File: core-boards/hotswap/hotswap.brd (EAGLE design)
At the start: 59.7 x 56.8 mm, 16 parts, among them J1 WALL, J2 BATTERY, J3 COMPUTER, Q1 SUP75P03_07, Q2 SUP75P03_07, Q3 SUP75P03_07, U1 LTC4416EMS#PBF

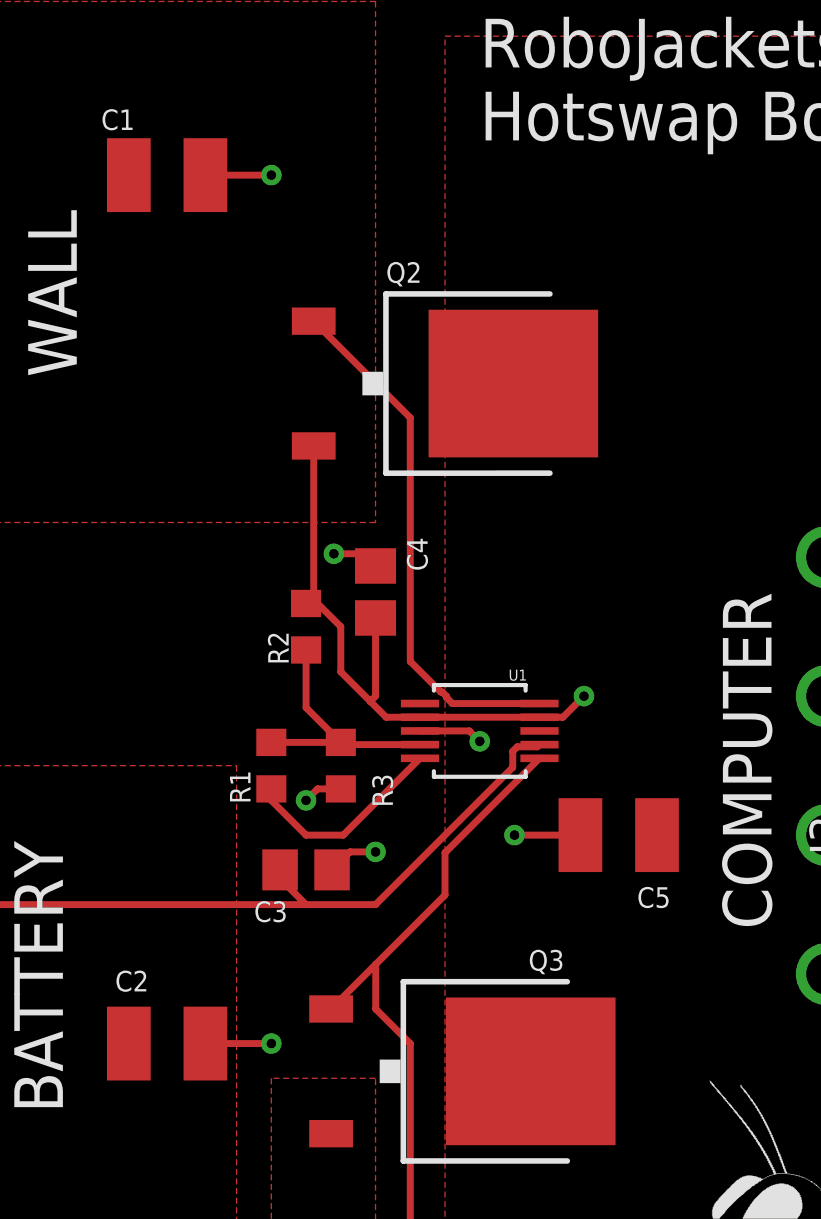
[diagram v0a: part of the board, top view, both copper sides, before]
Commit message: Flip transistor sides so voltage does not reverse flow from V2 to V1 when V2 is higher
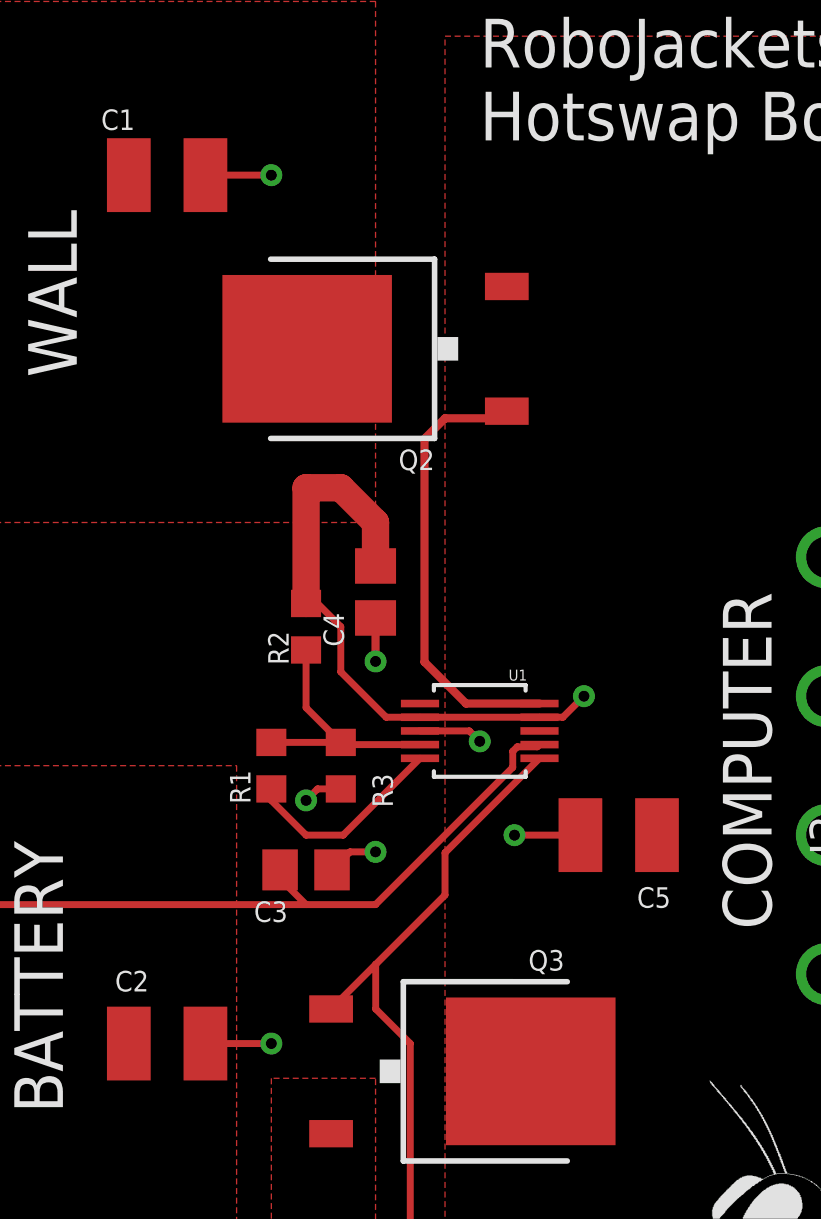
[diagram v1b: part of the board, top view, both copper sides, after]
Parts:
- moved Q2 2.84 mm to (29.2, 44.5), turned to 90 degrees
- turned C4 to 270 degrees
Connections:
- net VCC_COMP: now also Q2.S; no longer Q2.D
- net VCC_WALL: now also Q2.D; no longer Q2.S
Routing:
- net N$4: track 19.3 -> 16.4 mm
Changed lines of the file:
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@@
 <?xml version="1.0" encoding="utf-8"?>
 <!DOCTYPE eagle SYSTEM "eagle.dtd">
-<eagle version="9.3.0">
+<eagle version="9.4.2">
 <drawing>
 <settings>
@@
 <setting verticaltext="up"/>
 </settings>
-<grid distance="50" unitdist="mil" unit="mm" style="lines" multiple="1" display="no" altdistance="5" altunitdist="mil" altunit="mm"/>
+<grid distance="1" unitdist="mm" unit="mm" style="lines" multiple="1" display="no" altdistance="1" altunitdist="mm" altunit="mm"/>
 <layers>
 <layer number="1" name="Top" color="4" fill="1" visible="yes" active="yes"/>
@@
 <attribute name="SPICEPREFIX" value="R" x="154.94" y="71.12" size="1.778" layer="27" rot="R90" display="off"/>
 </element>
-<element name="Q2" library="IGVC-Discrete" package="DPACK_2" value="SUP75P03_07" x="31.75" y="43.18" smashed="yes" rot="R270">
-<attribute name="NAME" x="29.591" y="46.863" size="0.75" layer="25"/>
+<element name="Q2" library="IGVC-Discrete" package="DPACK_2" value="SUP75P03_07" x="29.21" y="44.45" smashed="yes" rot="R90">
+<attribute name="NAME" x="31.369" y="40.767" size="0.75" layer="25" rot="R180"/>
 </element>
 <element name="Q3" library="IGVC-Discrete" package="DPACK_2" value="SUP75P03_07" x="32.385" y="18.034" smashed="yes" rot="R270">
@@
 <attribute name="SPICEPREFIX" value="C" x="38.1" y="26.67" size="1.778" layer="27" rot="R180" display="off"/>
 </element>
-<element name="C4" library="rcl" library_urn="urn:adsk.eagle:library:334" package="C0805" package3d_urn="urn:adsk.eagle:package:23617/2" value=".1uF" x="29.21" y="35.56" smashed="yes" rot="R90">
-<attribute name="NAME" x="31.115" y="36.322" size="0.75" layer="25" rot="R90"/>
-<attribute name="SPICEPREFIX" value="C" x="29.21" y="35.56" size="1.778" layer="27" rot="R90" display="off"/>
+<element name="C4" library="rcl" library_urn="urn:adsk.eagle:library:334" package="C0805" package3d_urn="urn:adsk.eagle:package:23617/2" value=".1uF" x="29.21" y="35.56" smashed="yes" rot="R270">
+<attribute name="NAME" x="27.305" y="34.798" size="0.75" layer="25" rot="R270"/>
+<attribute name="SPICEPREFIX" value="C" x="29.21" y="35.56" size="1.778" layer="27" rot="R270" display="off"/>
 </element>
 <element name="E$1" library="RoboJackets-Aesthetics" package="ROBOBUZZ_0.8X" value="" x="44.45" y="2.54" smashed="yes"/>
@@
 <wire x1="27.94" y1="28.36" x2="27.09" y2="28.36" width="0.254" layer="1"/>
 <wire x1="27.09" y1="28.36" x2="26.67" y2="27.94" width="0.254" layer="1"/>
-<via x="26.67" y="27.94" extent="1-16" drill="0.35"/>
+<via x="26.67" y="27.94" extent="1-16" drill="0.4"/>
 <wire x1="33.02" y1="30.099" x2="32.639" y2="30.48" width="0.254" layer="1"/>
 <wire x1="32.639" y1="30.48" x2="30.8356" y2="30.48" width="0.254" layer="1"/>
-<via x="33.02" y="30.099" extent="1-16" drill="0.35"/>
+<via x="33.02" y="30.099" extent="1-16" drill="0.4"/>
 <contactref element="C4" pad="2"/>
 <contactref element="J2" pad="4"/>
 <contactref element="J1" pad="4"/>
 <wire x1="36.7" y1="26.67" x2="34.29" y2="26.67" width="0.254" layer="1"/>
-<via x="34.29" y="26.67" extent="1-16" drill="0.35"/>
+<via x="34.29" y="26.67" extent="1-16" drill="0.4"/>
 <wire x1="29.21" y1="26.0576" x2="28.2776" y2="26.0576" width="0.254" layer="1"/>
 <wire x1="27.62" y1="25.4" x2="28.2776" y2="26.0576" width="0.254" layer="1"/>
-<via x="29.21" y="26.0576" extent="1-16" drill="0.35"/>
+<via x="29.21" y="26.0576" extent="1-16" drill="0.4"/>
 <wire x1="25.4" y1="19.05" x2="22.99" y2="19.05" width="0.254" layer="1"/>
-<via x="25.4" y="19.05" extent="1-16" drill="0.35"/>
+<via x="25.4" y="19.05" extent="1-16" drill="0.4"/>
 <wire x1="22.99" y1="50.8" x2="25.4" y2="50.8" width="0.254" layer="1"/>
-<via x="25.4" y="50.8" extent="1-16" drill="0.35"/>
-<via x="27.686" y="36.957" extent="1-16" drill="0.35"/>
-<wire x1="29.21" y1="36.51" x2="28.763" y2="36.957" width="0.254" layer="1"/>
-<wire x1="28.763" y1="36.957" x2="27.686" y2="36.957" width="0.254" layer="1"/>
+<via x="25.4" y="50.8" extent="1-16" drill="0.4"/>
 <contactref element="C3" pad="2"/>
+<wire x1="29.21" y1="34.61" x2="29.21" y2="33.02" width="0.3" layer="1"/>
+<via x="29.21" y="33.02" extent="1-16" drill="0.4"/>
 </signal>
 <signal name="N$4">
 <contactref element="U1" pad="10"/>
 <contactref element="Q2" pad="G"/>
-<wire x1="26.95" y1="45.46" x2="30.48" y2="41.93" width="0.254" layer="1"/>
-<wire x1="30.48" y1="41.93" x2="30.48" y2="33.02" width="0.254" layer="1"/>
-<wire x1="32.019240625" y1="31.480759375" x2="35.2044" y2="31.480759375" width="0.254" layer="1"/>
-<wire x1="30.48" y1="33.02" x2="31.60014375" y2="31.89985625" width="0.254" layer="1"/>
-<wire x1="31.60014375" y1="31.89985625" x2="31.64983125" y2="31.89985625" width="0.254" layer="1"/>
-<wire x1="31.64983125" y1="31.89985625" x2="31.8135" y2="31.7361875" width="0.254" layer="1"/>
-<wire x1="31.8135" y1="31.7361875" x2="31.8135" y2="31.6865" width="0.254" layer="1"/>
-<wire x1="31.8135" y1="31.6865" x2="32.019240625" y2="31.480759375" width="0.254" layer="1"/>
+<wire x1="34.01" y1="42.17" x2="33.75" y2="41.91" width="0.3" layer="1"/>
+<wire x1="33.75" y1="41.91" x2="31.75" y2="41.91" width="0.3" layer="1"/>
+<wire x1="31.75" y1="41.91" x2="31" y2="41.16" width="0.3" layer="1"/>
+<wire x1="31" y1="33" x2="32.519240625" y2="31.480759375" width="0.3" layer="1"/>
+<wire x1="32.519240625" y1="31.480759375" x2="35.2044" y2="31.480759375" width="0.3" layer="1"/>
+<wire x1="31" y1="41.16" x2="31" y2="33" width="0.3" layer="1"/>
 </signal>
 <signal name="N$9">
@@
 </signal>
 <signal name="VCC_WALL">
-<contactref element="Q2" pad="S"/>
 <contactref element="U1" pad="9"/>
 <contactref element="U1" pad="2"/>
@@
 </polygon>
 <wire x1="26.67" y1="35.14" x2="26.88" y2="35.35" width="0.254" layer="1"/>
-<wire x1="26.88" y1="35.35" x2="26.95" y2="35.42" width="0.254" layer="1"/>
-<wire x1="26.95" y1="35.42" x2="26.95" y2="40.9" width="0.254" layer="1"/>
 <wire x1="35.2044" y1="30.98038125" x2="36.06038125" y2="30.98038125" width="0.254" layer="1"/>
 <wire x1="36.06038125" y1="30.98038125" x2="36.83" y2="31.75" width="0.254" layer="1"/>
-<via x="36.83" y="31.75" extent="1-16" drill="0.35"/>
+<via x="36.83" y="31.75" extent="1-16" drill="0.4"/>
 <wire x1="27.94" y1="32.639" x2="27.94" y2="34.29" width="0.254" layer="1"/>
 <wire x1="27.94" y1="34.29" x2="26.88" y2="35.35" width="0.254" layer="1"/>
 <wire x1="35.2044" y1="30.98038125" x2="30.8356" y2="30.98038125" width="0.254" layer="1"/>
 <wire x1="30.8356" y1="30.98038125" x2="29.59861875" y2="30.98038125" width="0.254" layer="1"/>
-<wire x1="29.59861875" y1="30.98038125" x2="29.0195" y2="31.5595" width="0.254" layer="1"/>
 <contactref element="J1" pad="1"/>
 <contactref element="C1" pad="1"/>
 <contactref element="C4" pad="1"/>
 <contactref element="J1" pad="2"/>
-<wire x1="29.0195" y1="31.5595" x2="27.94" y2="32.639" width="0.254" layer="1"/>
-<wire x1="29.0195" y1="31.5595" x2="29.21" y2="31.75" width="0.254" layer="1"/>
-<wire x1="29.21" y1="31.75" x2="29.21" y2="34.61" width="0.254" layer="1"/>
+<wire x1="29.59861875" y1="30.98038125" x2="27.94" y2="32.639" width="0.254" layer="1"/>
+<contactref element="Q2" pad="D"/>
+<wire x1="26.67" y1="35.14" x2="26.67" y2="39.37" width="1" layer="1"/>
+<wire x1="26.67" y1="39.37" x2="27.94" y2="39.37" width="1" layer="1"/>
+<wire x1="27.94" y1="39.37" x2="29.21" y2="38.1" width="1" layer="1"/>
+<wire x1="29.21" y1="38.1" x2="29.21" y2="36.51" width="1" layer="1"/>
 </signal>
 <signal name="N$1">
@@
 <signal name="VCC_COMP">
 <contactref element="U1" pad="8"/>
-<contactref element="Q2" pad="D"/>
 <polygon width="0.254" layer="1" thermals="no">
 <vertex x="58.42" y="55.88"/>
@@
 <contactref element="C5" pad="1"/>
 <contactref element="Q3" pad="D"/>
+<contactref element="Q2" pad="S"/>
 </signal>
 <signal name="VCC_BATT">

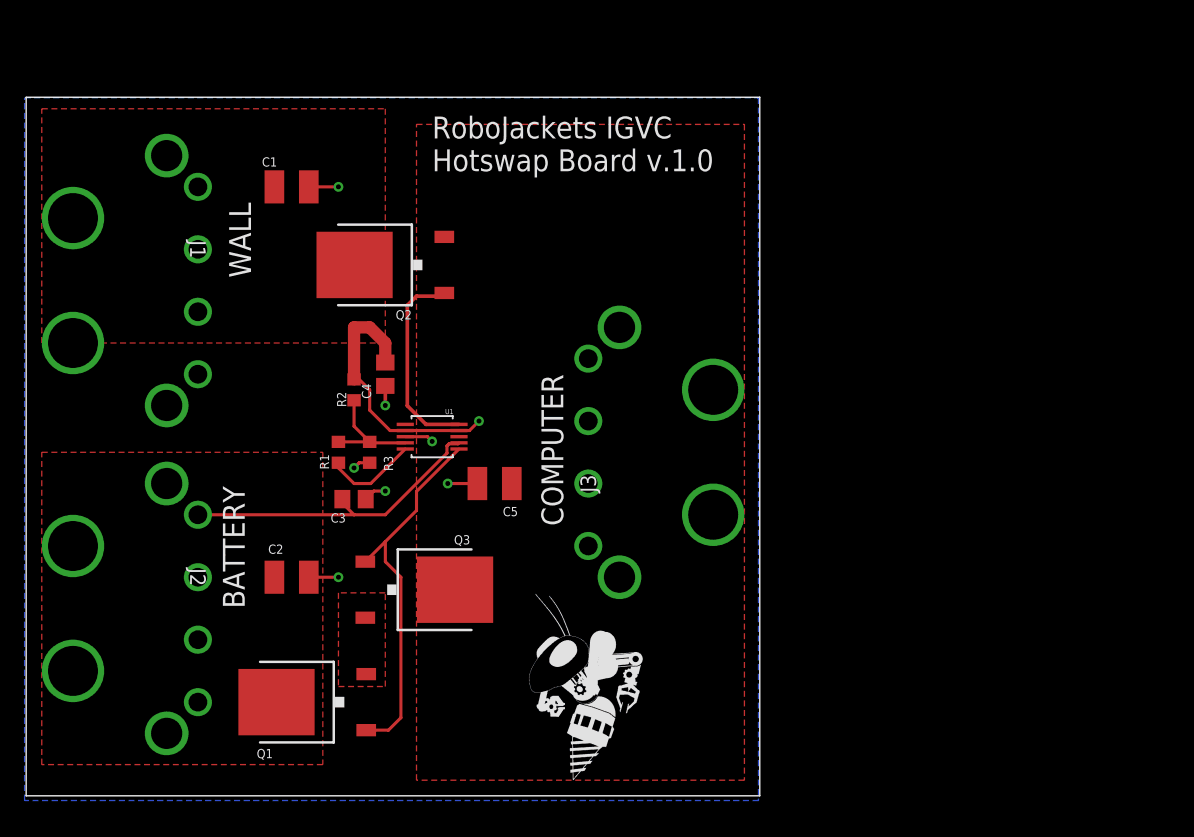
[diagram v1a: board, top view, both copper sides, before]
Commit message: Added new connector
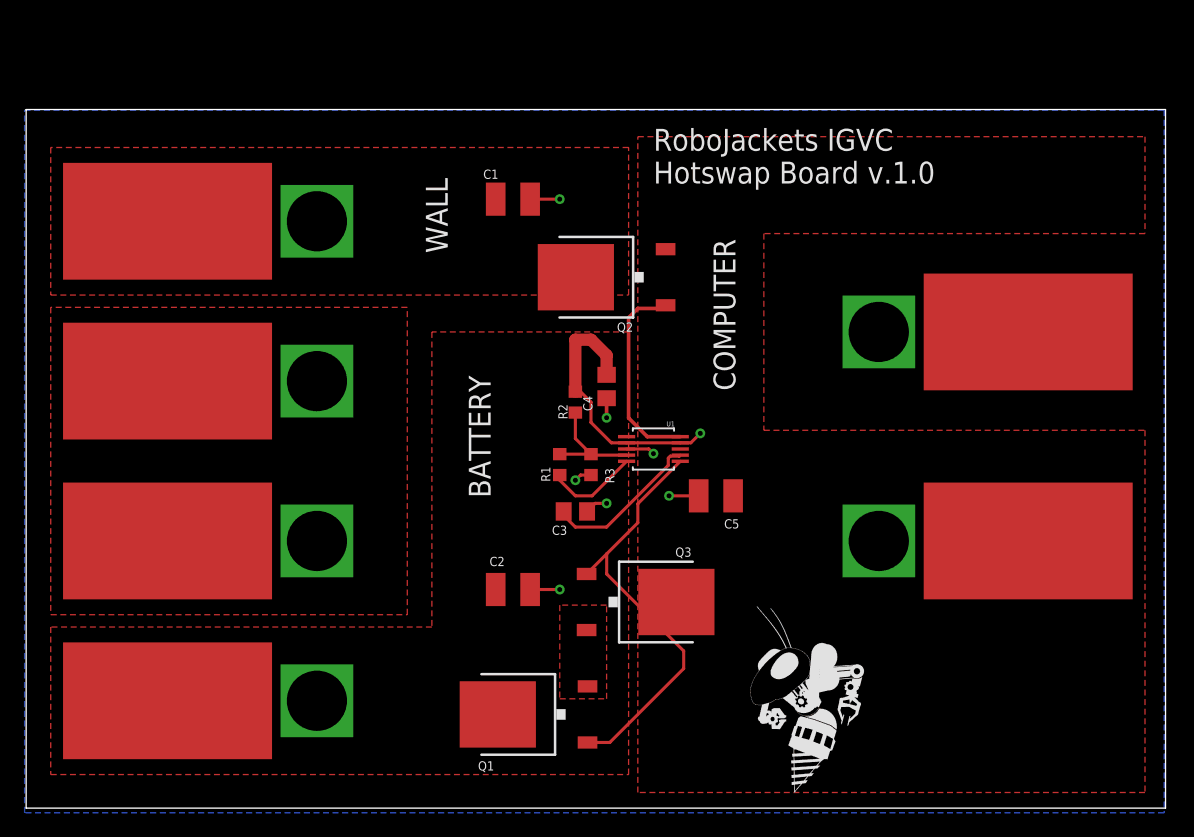
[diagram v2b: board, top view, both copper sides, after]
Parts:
- removed J1: WALL, IGVC-Connector:641737-1
- removed J2: BATTERY, IGVC-Connector:641737-1
- removed J3: COMPUTER, IGVC-Connector:641737-1
- added U$1, U$2, U$3, U$4, U$5, U$6: 6T4AWGLUG, IGVC-Connector:6T4AWGLUG
- moved C1 18.0 mm to (39.6, 49.8)
- moved C2 18.0 mm to (39.6, 18.1)
- moved C3 18.0 mm to (44.7, 24.4)
- moved C4 18.0 mm to (47.2, 34.6)
- moved C5 18.0 mm to (56.1, 25.7)
- moved E$1 18.0 mm to (62.5, 1.54)
- moved Q1 18.0 mm to (40.9, 7.89)
- moved Q2 18.0 mm to (47.2, 43.5)
- moved Q3 18.0 mm to (50.4, 17.0)
- moved R1 18.0 mm to (43.4, 28.2)
- moved R2 18.0 mm to (44.7, 33.3)
- moved U1 18.0 mm to (51.0, 29.5)
- moved R3 18.0 mm to (45.9, 28.2)
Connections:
- net GND: now also U$1.P$1, U$1.P$2, U$2.P$1, U$2.P$2, U$5.P$1, U$5.P$2; no longer J1.3, J1.4, J2.3, J2.4, J3.3, J3.4
- net VCC_BATT: now also U$3.P$1, U$3.P$2; no longer J2.1, J2.2
- net VCC_COMP: now also U$6.P$1, U$6.P$2; no longer J3.1, J3.2
- net VCC_WALL: now also U$4.P$1, U$4.P$2; no longer J1.1, J1.2
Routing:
- net VCC_BATT: track 25.7 -> 13.0 mm
- net N$3: track 30.4 -> 34.6 mm
- added copper zone on layer 1, net GND
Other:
- board size 59.7 x 56.8 mm -> 92.7 x 56.8 mm

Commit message: Routed the Board
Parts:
- removed U$5: 6T4AWGLUG, IGVC-Connector:6T4AWGLUG
- added VCC_COMP: 6T4AWGLUG, IGVC-Connector:6T4AWGLUG
- moved R2 14.9 mm to (34.7, 44.3)
- moved C4 12.8 mm to (39.2, 44.6)
- moved U$6 2.24 mm to (84.0, 20.0)
- renumbered U$3 to VCC_BATT, U$4 to VCC_WALL
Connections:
- net GND: now also VCC_COMP.P$1, VCC_COMP.P$2; no longer U$5.P$1, U$5.P$2
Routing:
- net GND: track 14.5 -> 39.9 mm
- net N$5: track 9.37 -> 24.5 mm
- net VCC_WALL: track 22.2 -> 29.2 mm
- net N$3: track 34.6 -> 28.3 mm
- net N$1: track 0.00 -> 4.62 mm
- removed copper zone on layer 1, net N$1
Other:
- board text added: "GND"
